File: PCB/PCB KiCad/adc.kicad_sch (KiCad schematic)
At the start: 18 parts, among them U2 ADS1256IDBT, Y1 7.68MHz

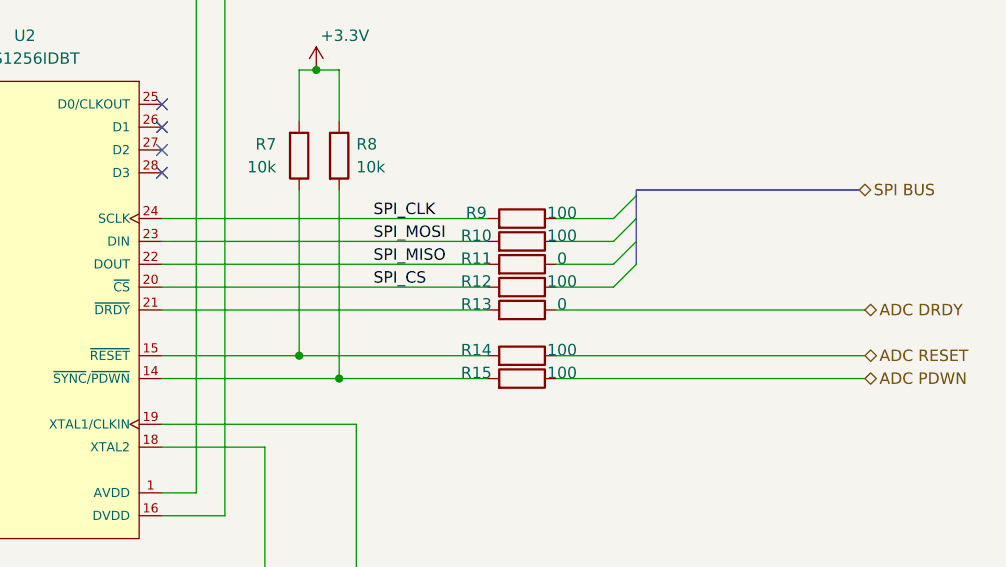
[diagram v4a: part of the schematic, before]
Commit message: Satisfy the overdemanding attention hungry ERC monster
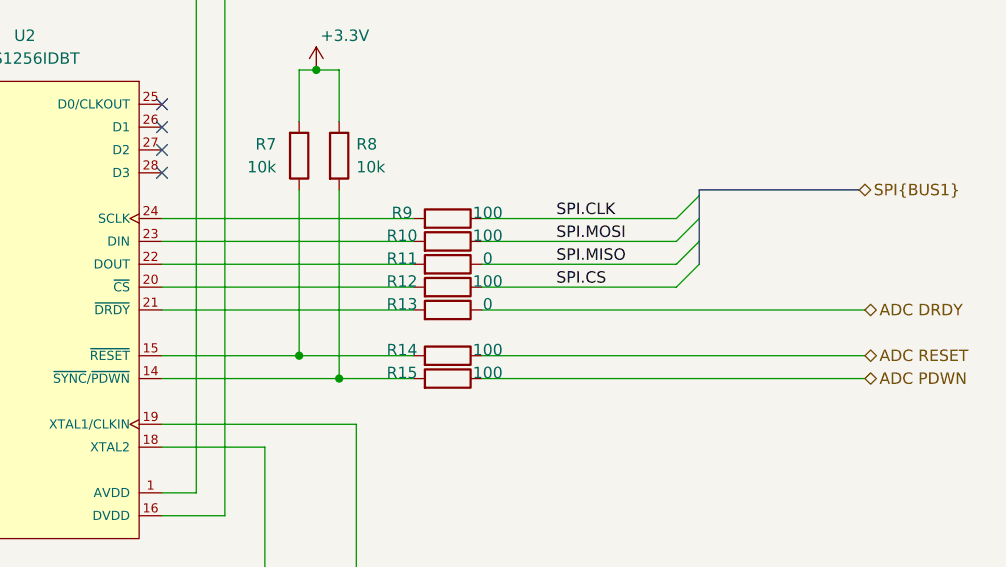
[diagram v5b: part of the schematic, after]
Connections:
- net SPI.CS: now reaches R12.1
- net SPI.MOSI: now reaches R10.1
- net SPI.MISO: now reaches R11.1
- net SPI.CLK: now reaches R9.1
- net SPI_CLK: no longer names the net of R9.2, U2.24 (SCLK)
- net SPI_CS: no longer names the net of R12.2, U2.20 (~{CS})
- net SPI_MISO: no longer names the net of R11.2, U2.22 (DOUT)
- net SPI_MOSI: no longer names the net of R10.2, U2.23 (DIN)
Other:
- moved on the sheet: R10, R11, R12, R13, R14, R15, R9

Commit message: Add footprints
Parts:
- R10, R11, R12, R13, R14, R15, R7, R8, R9: footprint (none) -> Resistor_SMD:R_0805_2012Metric_Pad1.20x1.40mm_HandSolder
- Y1: footprint (none) -> Crystal:Crystal_HC49-U_Vertical
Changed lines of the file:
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@@
     (property "Reference" "Y1" (id 0) (at 189.23 124.46 0))
     (property "Value" "7.68MHz" (id 1) (at 189.23 127 0))
-    (property "Footprint" "" (id 2) (at 189.23 132.08 0)
+    (property "Footprint" "Crystal:Crystal_HC49-U_Vertical" (id 2) (at 189.23 132.08 0)
       (effects (font (size 1.27 1.27)) hide)
     )
@@
       (effects (font (size 1.27 1.27)) (justify left))
     )
-    (property "Footprint" "" (id 2) (at 190.627 75.565 90)
+    (property "Footprint" "Resistor_SMD:R_0805_2012Metric_Pad1.20x1.40mm_HandSolder" (id 2) (at 190.627 75.565 90)
       (effects (font (size 1.27 1.27)) hide)
     )
@@
       (effects (font (size 1.27 1.27)) (justify right))
     )
-    (property "Footprint" "" (id 2) (at 186.182 75.565 90)
+    (property "Footprint" "Resistor_SMD:R_0805_2012Metric_Pad1.20x1.40mm_HandSolder" (id 2) (at 186.182 75.565 90)
       (effects (font (size 1.27 1.27)) hide)
     )
@@
     (property "Reference" "R12" (id 0) (at 199.39 89.535 90))
     (property "Value" "100" (id 1) (at 208.915 89.535 90))
-    (property "Footprint" "" (id 2) (at 204.47 91.948 90)
+    (property "Footprint" "Resistor_SMD:R_0805_2012Metric_Pad1.20x1.40mm_HandSolder" (id 2) (at 204.47 91.948 90)
       (effects (font (size 1.27 1.27)) hide)
     )
@@
     (property "Reference" "R14" (id 0) (at 199.39 97.155 90))
     (property "Value" "100" (id 1) (at 208.915 97.155 90))
-    (property "Footprint" "" (id 2) (at 204.47 99.568 90)
+    (property "Footprint" "Resistor_SMD:R_0805_2012Metric_Pad1.20x1.40mm_HandSolder" (id 2) (at 204.47 99.568 90)
       (effects (font (size 1.27 1.27)) hide)
     )
@@
     (property "Reference" "R15" (id 0) (at 199.39 99.695 90))
     (property "Value" "100" (id 1) (at 208.915 99.695 90))
-    (property "Footprint" "" (id 2) (at 204.47 102.108 90)
+    (property "Footprint" "Resistor_SMD:R_0805_2012Metric_Pad1.20x1.40mm_HandSolder" (id 2) (at 204.47 102.108 90)
       (effects (font (size 1.27 1.27)) hide)
     )
@@
     (property "Reference" "R10" (id 0) (at 199.39 84.455 90))
     (property "Value" "100" (id 1) (at 208.915 84.455 90))
-    (property "Footprint" "" (id 2) (at 204.47 86.868 90)
+    (property "Footprint" "Resistor_SMD:R_0805_2012Metric_Pad1.20x1.40mm_HandSolder" (id 2) (at 204.47 86.868 90)
       (effects (font (size 1.27 1.27)) hide)
     )
@@
     (property "Reference" "R13" (id 0) (at 199.39 92.075 90))
     (property "Value" "0" (id 1) (at 208.915 92.075 90))
-    (property "Footprint" "" (id 2) (at 204.47 94.488 90)
+    (property "Footprint" "Resistor_SMD:R_0805_2012Metric_Pad1.20x1.40mm_HandSolder" (id 2) (at 204.47 94.488 90)
       (effects (font (size 1.27 1.27)) hide)
     )
@@
     (property "Reference" "R11" (id 0) (at 199.39 86.995 90))
     (property "Value" "0" (id 1) (at 208.915 86.995 90))
-    (property "Footprint" "" (id 2) (at 204.47 89.408 90)
+    (property "Footprint" "Resistor_SMD:R_0805_2012Metric_Pad1.20x1.40mm_HandSolder" (id 2) (at 204.47 89.408 90)
       (effects (font (size 1.27 1.27)) hide)
     )
@@
     (property "Reference" "R9" (id 0) (at 199.39 81.915 90))
     (property "Value" "100" (id 1) (at 208.915 81.915 90))
-    (property "Footprint" "" (id 2) (at 204.47 84.328 90)
-      (effects (font (size 1.27 1.27)) hide)
-    )
+    (property "Footprint" "Resistor_SMD:R_0805_2012Metric_Pad1.20x1.40mm_HandSolder" (id 2) (at 204.47 84.328 90)
+      (effects (font (size 1.27 1.27)) hide)
+    )
